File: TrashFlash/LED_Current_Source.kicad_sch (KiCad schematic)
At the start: 32 parts, among them IC2 ADG5419BCPZ-RL7, IC4 SN74LXC2T45QDTTRQ1, IC8 AD8615AUJZ-REEL, Q1 BC56-10PA,115, Q2 BC56-10PA,115, Q3 BC56-10PA,115, Q4 BC56-10PA,115, U1 SI5448DU-T1-GE3, U2 SI5448DU-T1-GE3

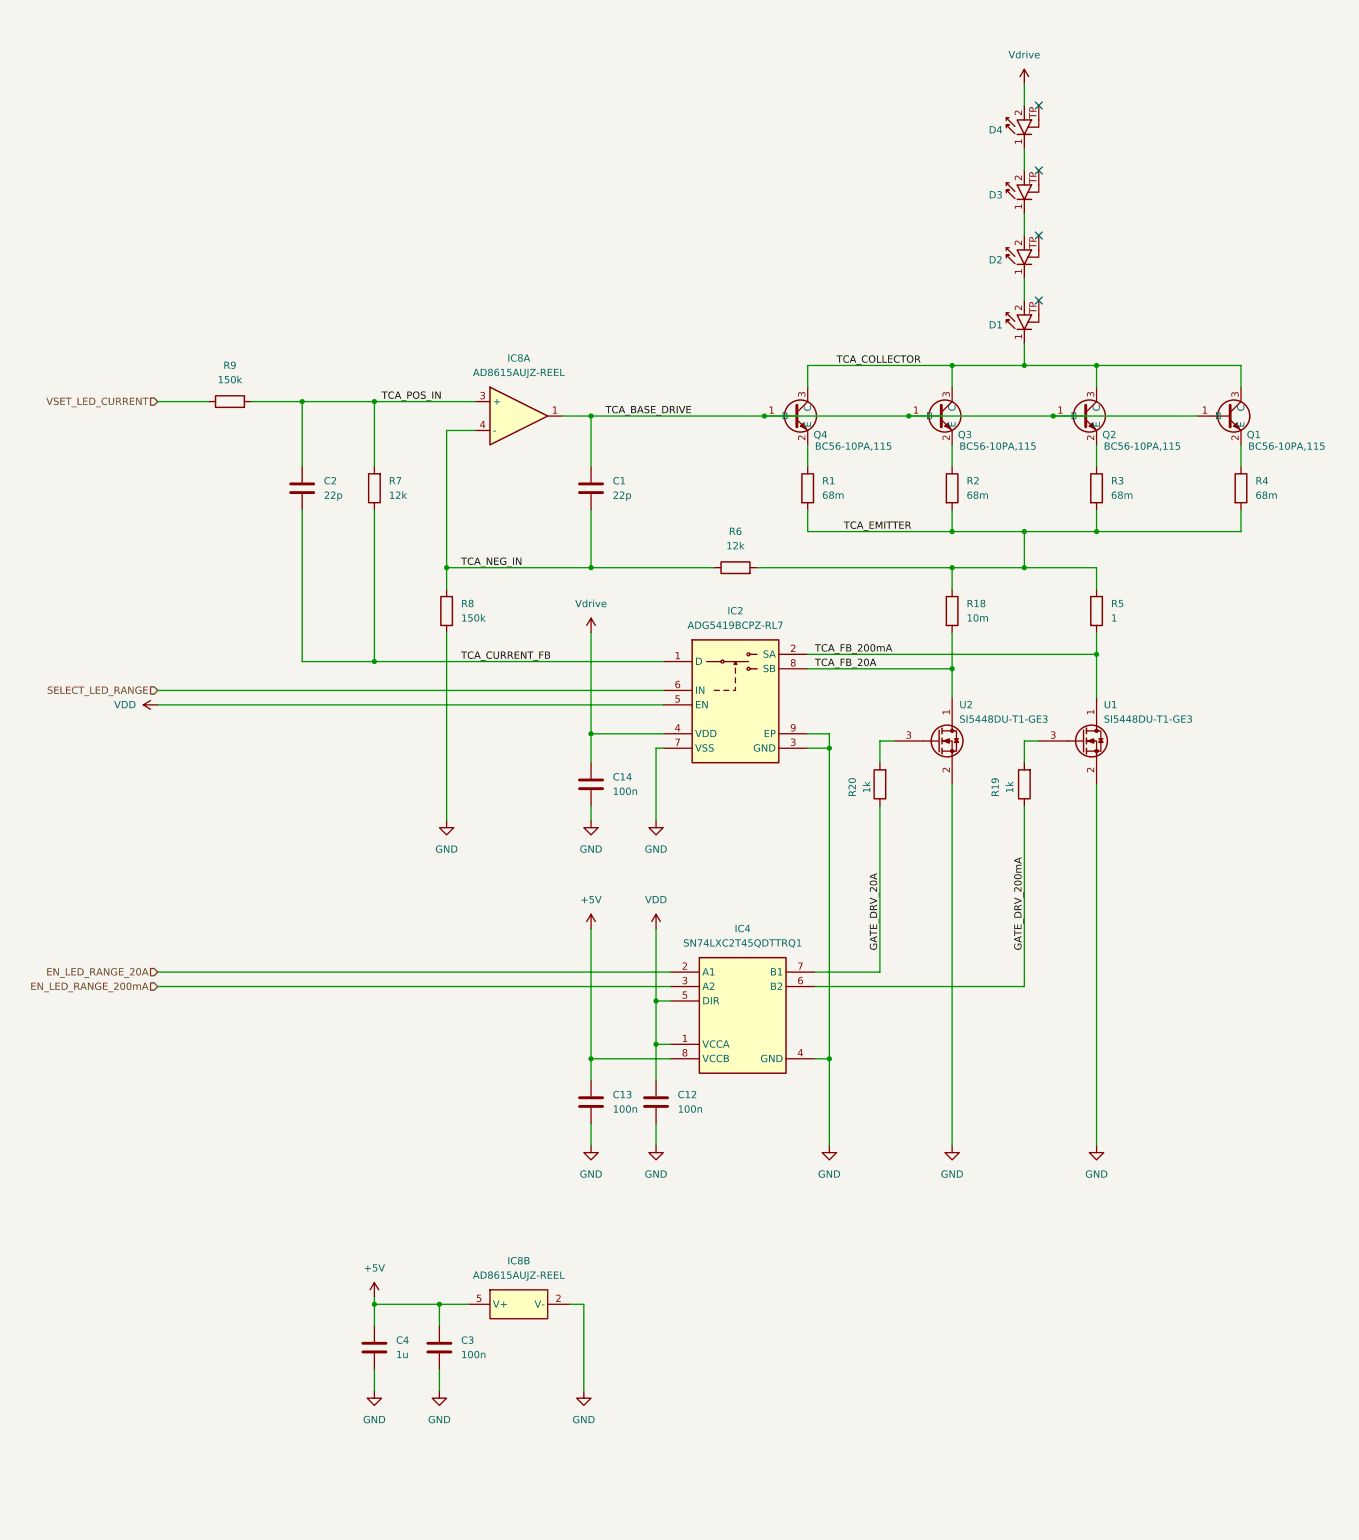
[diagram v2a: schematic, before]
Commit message: Added Wireless and inter PCB connector
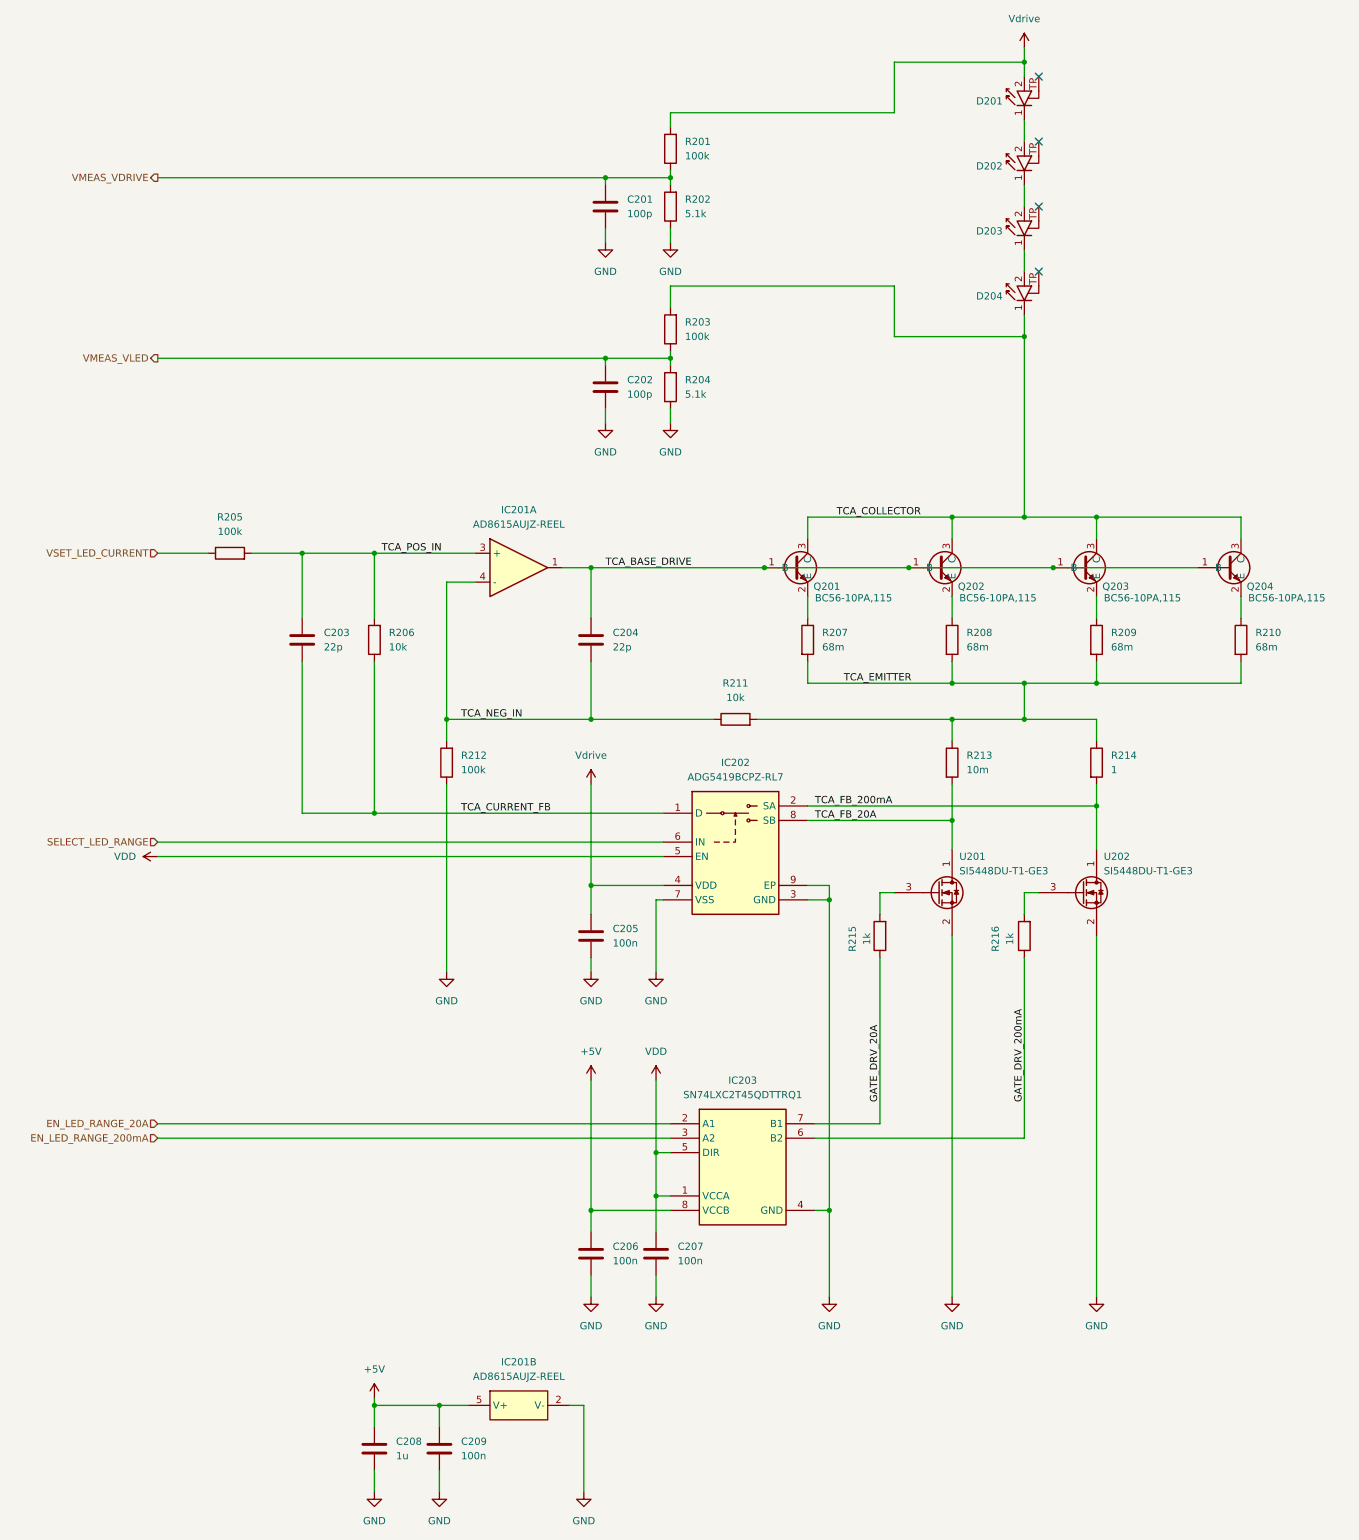
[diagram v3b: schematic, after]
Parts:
- added C201, C202: 100p, Capacitor_SMD:C_0402_1005Metric, symbol Device:C
- added R201, R203: 100k, Resistor_SMD:R_0402_1005Metric, symbol Device:R
- added R202, R204: 5.1k, Resistor_SMD:R_0402_1005Metric, symbol Device:R
- IC201: renamed from IC8; footprint TrashFlash:SOT95P280X100-5N -> SOT95P280X100-5N
- IC202: renamed from IC2; footprint TrashFlash:SON50P300X200X80-9N-D -> SON50P300X200X80-9N-D
- IC203: renamed from IC4; footprint TrashFlash:SN74LXC2T45QDTTRQ1 -> SN74LXC2T45QDTTRQ1
- Q201: renamed from Q4; footprint TrashFlash:PTVS24VZ1UPAZ -> PTVS24VZ1UPAZ
- Q202: renamed from Q3; footprint TrashFlash:PTVS24VZ1UPAZ -> PTVS24VZ1UPAZ
- Q203: renamed from Q2; footprint TrashFlash:PTVS24VZ1UPAZ -> PTVS24VZ1UPAZ
- Q204: renamed from Q1; footprint TrashFlash:PTVS24VZ1UPAZ -> PTVS24VZ1UPAZ
- R205: renamed from R9; value 150k -> 100k
- R206: renamed from R7; value 12k -> 10k
- R211: renamed from R6; value 12k -> 10k
- R212: renamed from R8; value 150k -> 100k
- R213: renamed from R18; footprint Resistor_SMD:R_0603_1608Metric -> Resistor_SMD:R_0805_2012Metric
- R214: renamed from R5; footprint Resistor_SMD:R_0603_1608Metric -> Resistor_SMD:R_0805_2012Metric
- U201: renamed from U2; footprint TrashFlash:SI5448DUT1GE3 -> SI5448DUT1GE3
- U202: renamed from U1; footprint TrashFlash:SI5448DUT1GE3 -> SI5448DUT1GE3
- renumbered C2 to C203, C1 to C204, C14 to C205, C13 to C206, C12 to C207, C4 to C208, C3 to C209, D4 to D201, D3 to D202, D2 to D203, D1 to D204, R1 to R207, R2 to R208, R3 to R209, R4 to R210, R20 to R215, R19 to R216
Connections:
- net GND: now also C201.2, C202.2, R202.1, R204.1
- net TCA_COLLECTOR: now also R203.2
- net Vdrive: now also R201.2
- new net VMEAS_VDRIVE: C201.1, R201.1, R202.2
- new net VMEAS_VLED: C202.1, R203.1, R204.2
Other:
- moved on the sheet: C203, C204, C205, C206, C207, C208, C209, D201, D202, D203, D204, IC201A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

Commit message: LED via stitch und han gmerkt das ich usversehe d batterie im letschte kommit use gno han sorry :)
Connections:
- net LED_TP: now reaches D204.TP
- net LED_TP: now also D201.TP, D202.TP, D203.TP
- no-connect marks 4 -> 0
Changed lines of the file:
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@@
+	)
+	(junction
+		(at 281.94 34.29)
+		(diameter 0)
+		(color 0 0 0 0)
 	)
 	(junction
@@
 	)
 	(junction
+		(at 281.94 45.72)
+		(diameter 0)
+		(color 0 0 0 0)
+	)
+	(junction
 		(at 175.26 137.16)
 		(diameter 0)
@@
 		(color 0 0 0 0)
 	)
-	(no_connect
-		(at 279.4 46.99)
-	)
-	(no_connect
-		(at 279.4 35.56)
-	)
-	(no_connect
-		(at 279.4 58.42)
-	)
-	(no_connect
-		(at 279.4 24.13)
-	)
 	(wire
 		(pts
@@
 	(wire
 		(pts
+			(xy 281.94 57.15) (xy 279.4 57.15)
+		)
+		(stroke
+			(width 0)
+			(type default)
+		)
+	)
+	(wire
+		(pts
 			(xy 175.26 148.59) (xy 175.26 181.61)
 		)
@@
 	(wire
 		(pts
+			(xy 279.4 57.15) (xy 279.4 58.42)
+		)
+		(stroke
+			(width 0)
+			(type default)
+		)
+	)
+	(wire
+		(pts
 			(xy 124.46 210.82) (xy 214.63 210.82)
 		)
@@
 	(wire
 		(pts
+			(xy 279.4 45.72) (xy 281.94 45.72)
+		)
+		(stroke
+			(width 0)
+			(type default)
+		)
+	)
+	(wire
+		(pts
 			(xy 200.66 166.37) (xy 213.36 166.37)
 		)
@@
 	(wire
 		(pts
+			(xy 279.4 22.86) (xy 281.94 22.86)
+		)
+		(stroke
+			(width 0)
+			(type default)
+		)
+	)
+	(wire
+		(pts
 			(xy 162.56 107.95) (xy 180.34 107.95)
 		)
@@
 	(wire
 		(pts
+			(xy 279.4 46.99) (xy 279.4 45.72)
+		)
+		(stroke
+			(width 0)
+			(type default)
+		)
+	)
+	(wire
+		(pts
 			(xy 214.63 85.09) (xy 214.63 82.55)
 		)
@@
 	(wire
 		(pts
+			(xy 279.4 24.13) (xy 279.4 22.86)
+		)
+		(stroke
+			(width 0)
+			(type default)
+		)
+	)
+	(wire
+		(pts
 			(xy 200.66 234.95) (xy 200.66 238.76)
 		)
@@
 	(wire
 		(pts
+			(xy 279.4 34.29) (xy 281.94 34.29)
+		)
+		(stroke
+			(width 0)
+			(type default)
+		)
+	)
+	(wire
+		(pts
 			(xy 289.56 115.57) (xy 289.56 119.38)
 		)
@@
 	(wire
 		(pts
+			(xy 281.94 34.29) (xy 281.94 45.72)
+		)
+		(stroke
+			(width 0)
+			(type default)
+		)
+	)
+	(wire
+		(pts
 			(xy 200.66 179.07) (xy 200.66 181.61)
 		)
@@
 	(wire
 		(pts
+			(xy 281.94 22.86) (xy 281.94 34.29)
+		)
+		(stroke
+			(width 0)
+			(type default)
+		)
+	)
+	(wire
+		(pts
 			(xy 203.2 41.91) (xy 214.63 41.91)
 		)
@@
 	(wire
 		(pts
+			(xy 281.94 45.72) (xy 281.94 57.15)
+		)
+		(stroke
+			(width 0)
+			(type default)
+		)
+	)
+	(wire
+		(pts
 			(xy 203.2 73.66) (xy 203.2 74.93)
 		)
@@
 		(pts
 			(xy 238.76 166.37) (xy 242.57 166.37)
+		)
+		(stroke
+			(width 0)
+			(type default)
+		)
+	)
+	(wire
+		(pts
+			(xy 279.4 35.56) (xy 279.4 34.29)
 		)
 		(stroke
@@
 		(effects
 			(font
+				(size 1.27 1.27)
+			)
+			(justify left bottom)
+		)
+	)
+	(label "LED_TP"
+		(at 281.94 22.86 0)
+		(effects
+			(font

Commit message: Added battery and connectors, Schematic remark for BQ297xx
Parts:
- IC201: footprint SOT95P280X100-5N -> TrashFlash:SOT95P280X100-5N
- IC202: footprint SON50P300X200X80-9N-D -> TrashFlash:SON50P300X200X80-9N-D
- IC203: footprint SN74LXC2T45QDTTRQ1 -> TrashFlash:SN74LXC2T45QDTTRQ1
- Q201, Q202, Q203, Q204: footprint PTVS24VZ1UPAZ -> TrashFlash:PTVS24VZ1UPAZ
- U201, U202: footprint SI5448DUT1GE3 -> TrashFlash:SI5448DUT1GE3
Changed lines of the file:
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@@
 			)
 		)
-		(property "Footprint" "SI5448DUT1GE3"
+		(property "Footprint" "TrashFlash:SI5448DUT1GE3"
 			(at 285.75 262.56 0)
 			(effects
@@
 			)
 		)
-		(property "Footprint" "SON50P300X200X80-9N-D"
+		(property "Footprint" "TrashFlash:SON50P300X200X80-9N-D"
 			(at 226.314 172.466 0)
 			(effects
@@
 			)
 		)
-		(property "Footprint" "SOT95P280X100-5N"
+		(property "Footprint" "TrashFlash:SOT95P280X100-5N"
 			(at 209.55 352.73 0)
 			(effects
@@
 			)
 		)
-		(property "Footprint" "PTVS24VZ1UPAZ"
+		(property "Footprint" "TrashFlash:PTVS24VZ1UPAZ"
 			(at 262.636 123.444 0)
 			(effects
@@
 			)
 		)
-		(property "Footprint" "PTVS24VZ1UPAZ"
+		(property "Footprint" "TrashFlash:PTVS24VZ1UPAZ"
 			(at 313.436 123.444 0)
 			(effects
@@
 			)
 		)
-		(property "Footprint" "SOT95P280X100-5N"
+		(property "Footprint" "TrashFlash:SOT95P280X100-5N"
 			(at 207.01 205.41 0)
 			(effects
@@
 			)
 		)
-		(property "Footprint" "SN74LXC2T45QDTTRQ1"
+		(property "Footprint" "TrashFlash:SN74LXC2T45QDTTRQ1"
 			(at 251.46 300.66 0)
 			(effects
@@
 			)
 		)
-		(property "Footprint" "PTVS24VZ1UPAZ"
+		(property "Footprint" "TrashFlash:PTVS24VZ1UPAZ"
 			(at 237.236 123.444 0)
 			(effects
@@
 			)
 		)
-		(property "Footprint" "PTVS24VZ1UPAZ"
+		(property "Footprint" "TrashFlash:PTVS24VZ1UPAZ"
 			(at 288.036 123.444 0)
 			(effects
@@
 			)
 		)
-		(property "Footprint" "SI5448DUT1GE3"
+		(property "Footprint" "TrashFlash:SI5448DUT1GE3"
 			(at 311.15 262.56 0)
 			(effects
